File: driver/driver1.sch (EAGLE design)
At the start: 86 parts, among them IC3 74HC14N, IC4 74HC08N, IC5 74HC74N

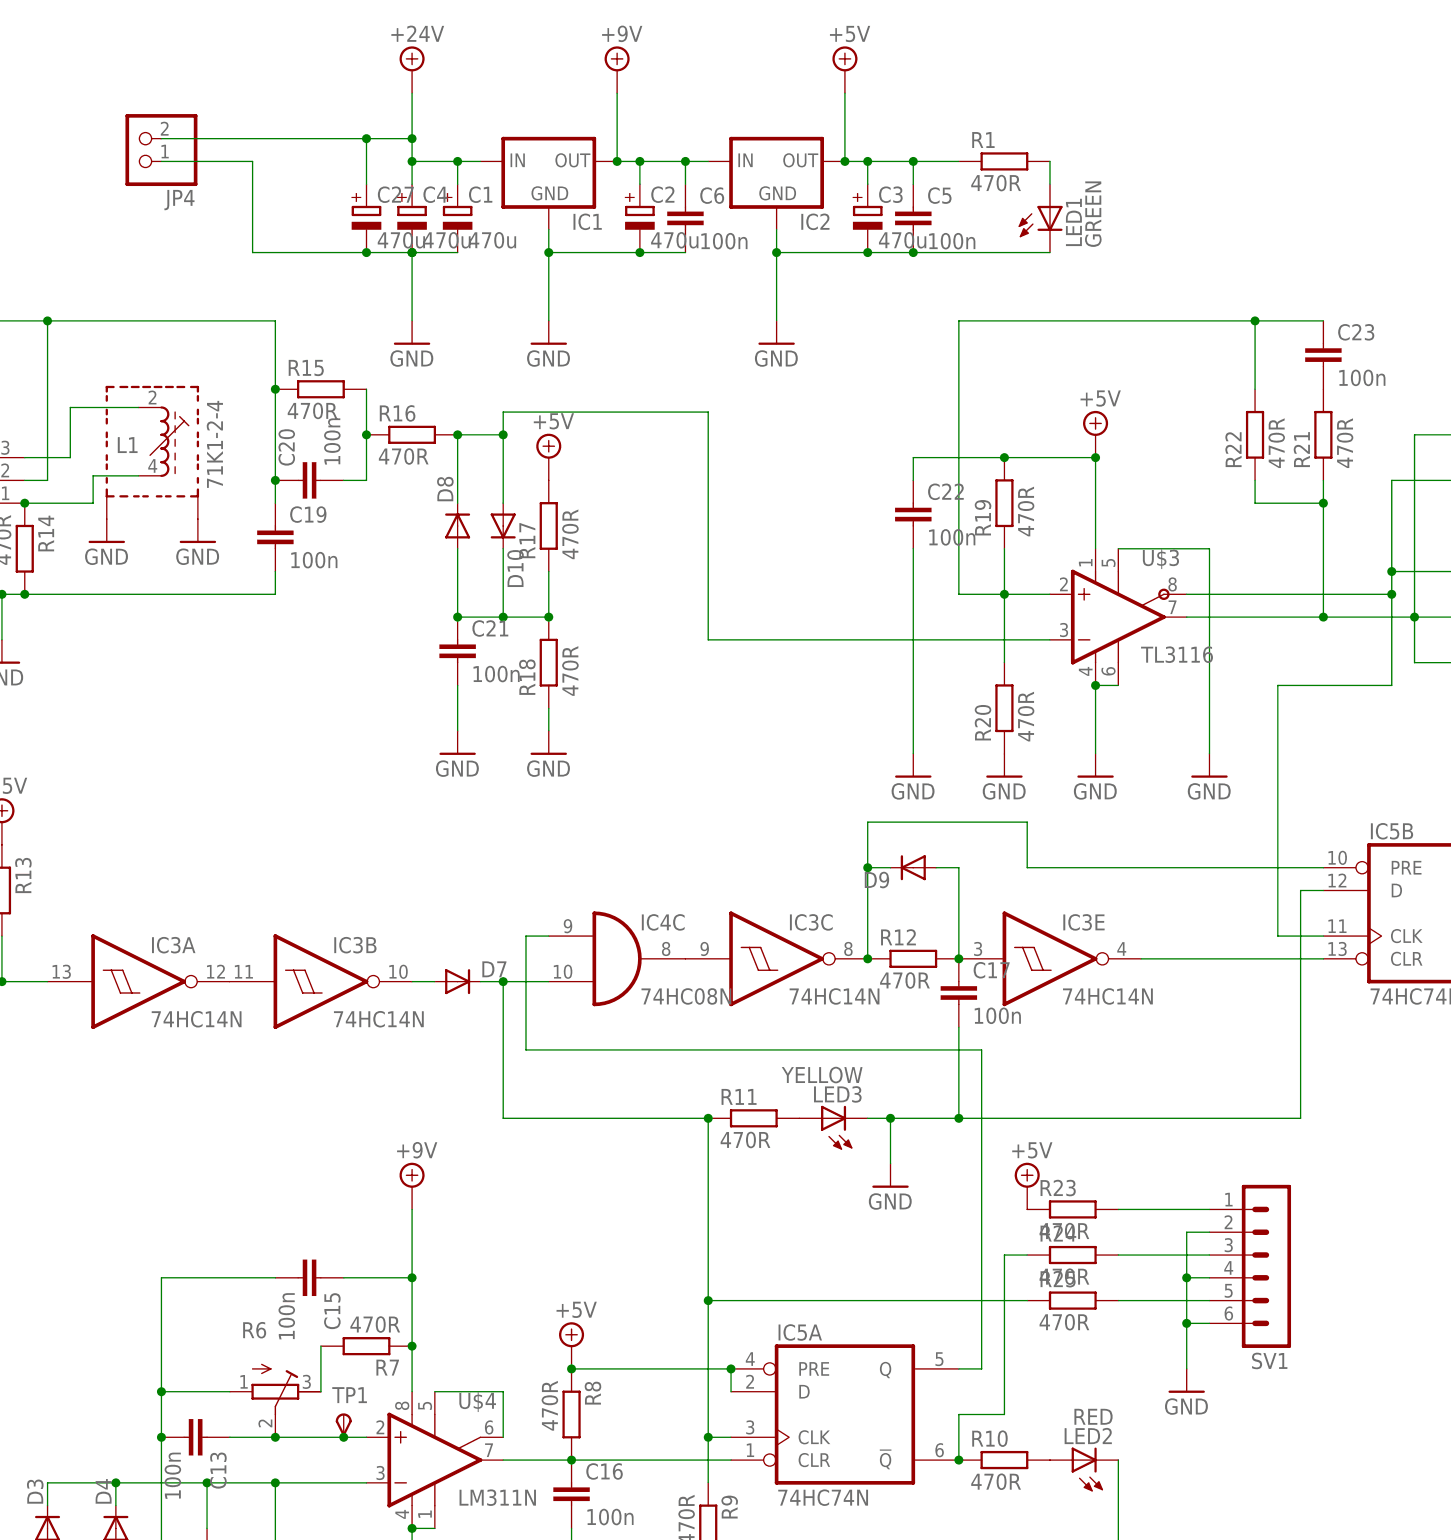
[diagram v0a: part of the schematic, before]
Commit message: improved board layout for use with recom switching 78xx regulators
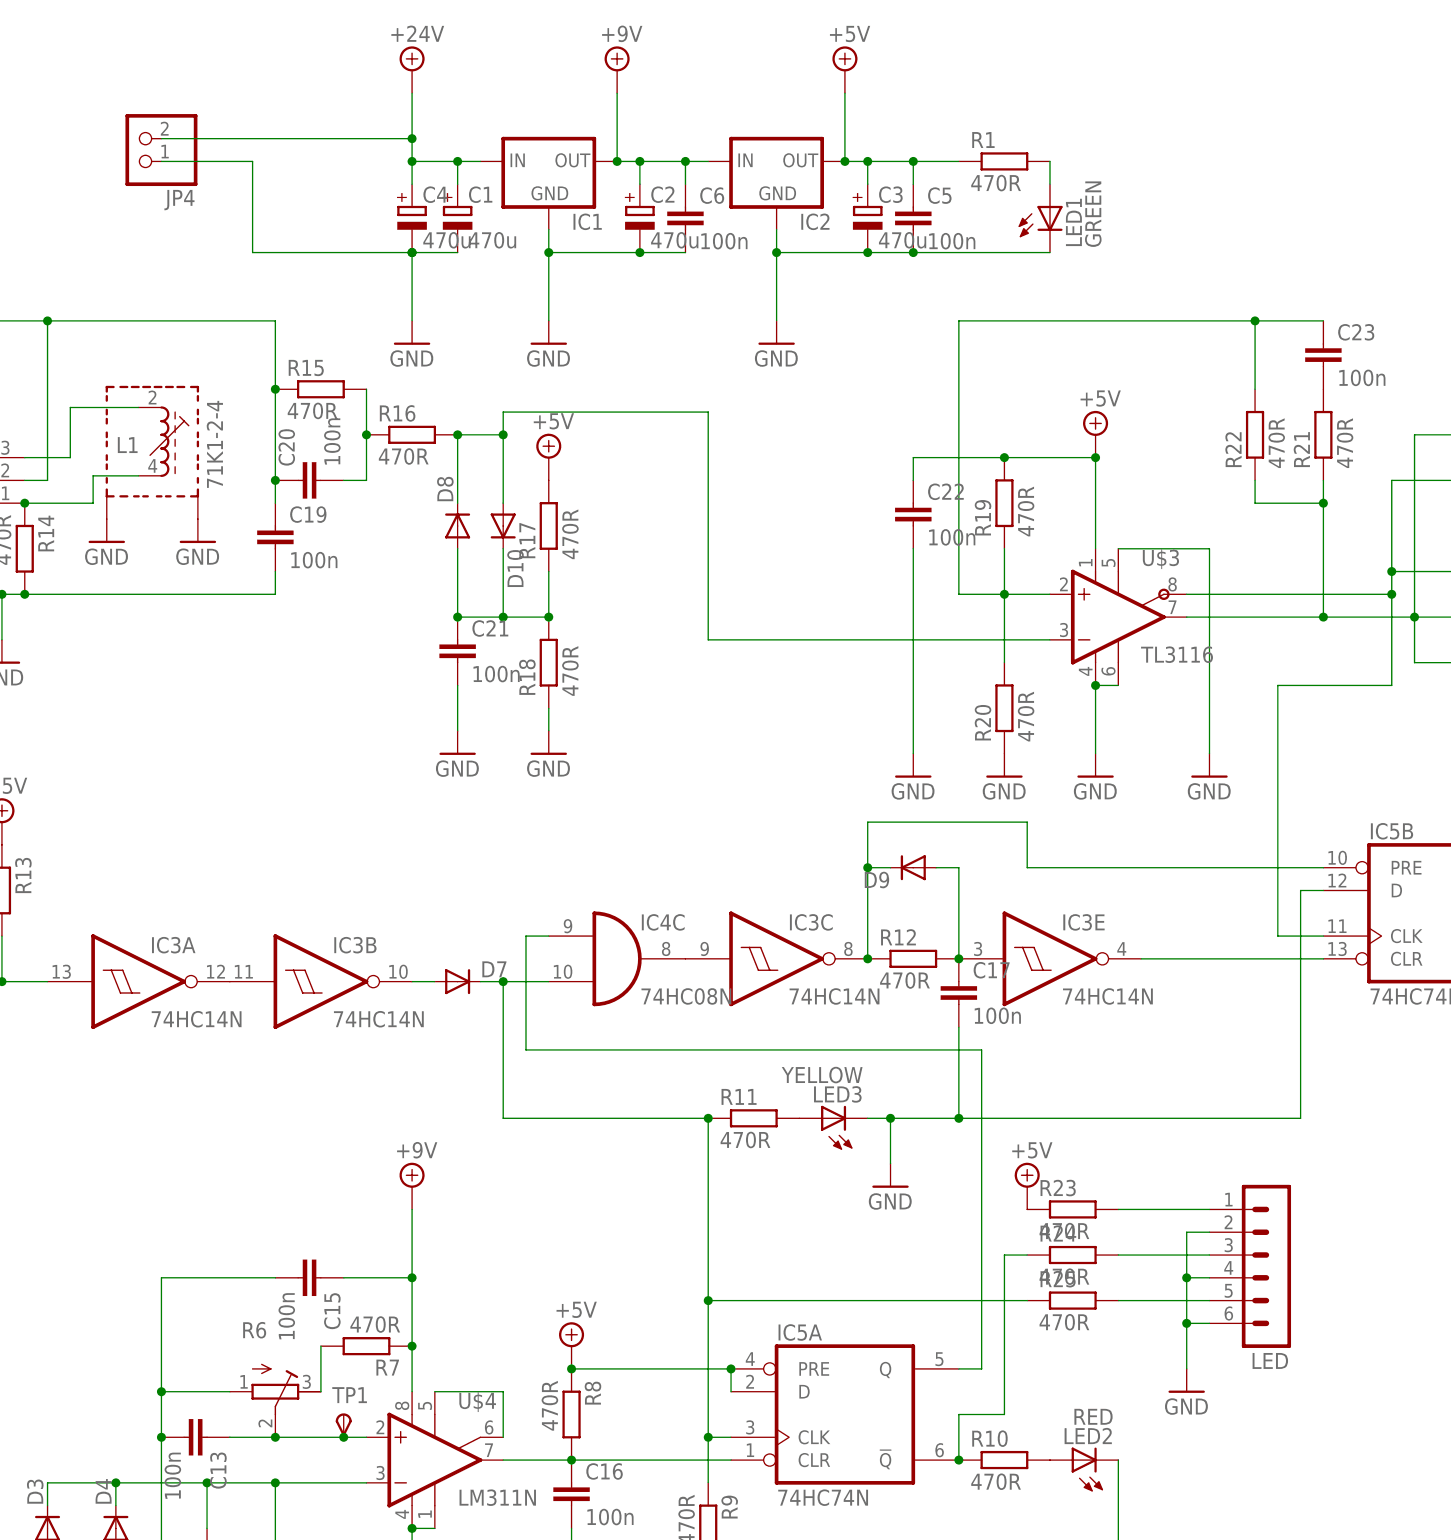
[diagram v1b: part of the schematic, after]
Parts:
- removed C27: 470u, rcl:CPOL-EUE5-8.5
- renumbered SV1 to LED
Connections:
- net +24V: no longer C27.+
- net GND: no longer C27.-
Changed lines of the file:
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@@
 <part name="GND30" library="supply1" deviceset="GND" device=""/>
 <part name="GND31" library="supply1" deviceset="GND" device=""/>
-<part name="SV1" library="con-lstb" deviceset="MA06-1" device=""/>
+<part name="LED" library="con-lstb" deviceset="MA06-1" device=""/>
 <part name="R23" library="rcl" deviceset="R-EU_" device="0207/7" value="470R"/>
 <part name="R24" library="rcl" deviceset="R-EU_" device="0207/7" value="470R"/>
@@
 <part name="GND32" library="supply1" deviceset="GND" device=""/>
 <part name="SUPPLY16" library="supply2" deviceset="+5V" device=""/>
-<part name="C27" library="rcl" deviceset="CPOL-EU" device="E5-8.5" value="470u"/>
 </parts>
 <sheets>
@@
 <instance part="GND30" gate="1" x="-11.176" y="71.882"/>
 <instance part="GND31" gate="1" x="-1.016" y="71.882"/>
-<instance part="SV1" gate="1" x="119.38" y="-10.16" rot="R180"/>
+<instance part="LED" gate="1" x="119.38" y="-10.16" rot="R180"/>
 <instance part="R23" gate="G$1" x="96.52" y="-2.54"/>
 <instance part="R24" gate="G$1" x="96.52" y="-7.62"/>
@@
 <instance part="GND32" gate="1" x="109.22" y="-22.86"/>
 <instance part="SUPPLY16" gate="+5V" x="91.44" y="0"/>
-<instance part="C27" gate="G$1" x="17.78" y="109.22"/>
 </instances>
 <busses>
@@
 <wire x1="-5.08" y1="114.3" x2="5.08" y2="114.3" width="0.1524" layer="91"/>
 <wire x1="5.08" y1="114.3" x2="5.08" y2="104.14" width="0.1524" layer="91"/>
-<wire x1="5.08" y1="104.14" x2="17.78" y2="104.14" width="0.1524" layer="91"/>
+<wire x1="5.08" y1="104.14" x2="22.86" y2="104.14" width="0.1524" layer="91"/>
 <junction x="22.86" y="104.14"/>
-<pinref part="C27" gate="G$1" pin="-"/>
-<wire x1="17.78" y1="104.14" x2="22.86" y2="104.14" width="0.1524" layer="91"/>
-<junction x="17.78" y="104.14"/>
 </segment>
 <segment>
@@
 </segment>
 <segment>
-<pinref part="SV1" gate="1" pin="2"/>
+<pinref part="LED" gate="1" pin="2"/>
 <wire x1="111.76" y1="-5.08" x2="109.22" y2="-5.08" width="0.1524" layer="91"/>
 <pinref part="GND32" gate="1" pin="GND"/>
 <wire x1="109.22" y1="-5.08" x2="109.22" y2="-10.16" width="0.1524" layer="91"/>
-<pinref part="SV1" gate="1" pin="6"/>
+<pinref part="LED" gate="1" pin="6"/>
 <wire x1="109.22" y1="-10.16" x2="109.22" y2="-15.24" width="0.1524" layer="91"/>
 <wire x1="109.22" y1="-15.24" x2="109.22" y2="-20.32" width="0.1524" layer="91"/>
 <wire x1="111.76" y1="-15.24" x2="109.22" y2="-15.24" width="0.1524" layer="91"/>
 <junction x="109.22" y="-15.24"/>
-<pinref part="SV1" gate="1" pin="4"/>
+<pinref part="LED" gate="1" pin="4"/>
 <wire x1="111.76" y1="-10.16" x2="109.22" y2="-10.16" width="0.1524" layer="91"/>
 <junction x="109.22" y="-10.16"/>
@@
 <junction x="27.94" y="114.3"/>
 <pinref part="JP4" gate="G$1" pin="2"/>
-<wire x1="-5.08" y1="116.84" x2="17.78" y2="116.84" width="0.1524" layer="91"/>
+<wire x1="-5.08" y1="116.84" x2="22.86" y2="116.84" width="0.1524" layer="91"/>
 <junction x="22.86" y="116.84"/>
-<pinref part="C27" gate="G$1" pin="+"/>
-<wire x1="17.78" y1="116.84" x2="22.86" y2="116.84" width="0.1524" layer="91"/>
-<wire x1="17.78" y1="116.84" x2="17.78" y2="111.76" width="0.1524" layer="91"/>
-<junction x="17.78" y="116.84"/>
 </segment>
 <segment>
@@
 <net name="N$15" class="0">
 <segment>
-<pinref part="SV1" gate="1" pin="1"/>
+<pinref part="LED" gate="1" pin="1"/>
 <pinref part="R23" gate="G$1" pin="2"/>
 <wire x1="111.76" y1="-2.54" x2="101.6" y2="-2.54" width="0.1524" layer="91"/>
@@
 <net name="N$16" class="0">
 <segment>
-<pinref part="SV1" gate="1" pin="3"/>
+<pinref part="LED" gate="1" pin="3"/>
 <pinref part="R24" gate="G$1" pin="2"/>
 <wire x1="111.76" y1="-7.62" x2="101.6" y2="-7.62" width="0.1524" layer="91"/>
@@
 <net name="N$18" class="0">
 <segment>
-<pinref part="SV1" gate="1" pin="5"/>
+<pinref part="LED" gate="1" pin="5"/>
 <pinref part="R25" gate="G$1" pin="2"/>
 <wire x1="111.76" y1="-12.7" x2="101.6" y2="-12.7" width="0.1524" layer="91"/>

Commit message: guess what.. pcb improvements
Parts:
- R14: device rcl:R-EU_0207/7 -> rcl:R-EU_0309/12
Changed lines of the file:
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@@
 <part name="C18" library="rcl" deviceset="C-EU" device="025-025X050" value="100n"/>
 <part name="GND16" library="supply1" deviceset="GND" device=""/>
-<part name="R14" library="rcl" deviceset="R-EU_" device="0207/7" value="470R"/>
+<part name="R14" library="rcl" deviceset="R-EU_" device="0309/12" value="470R"/>
 <part name="SV2" library="con-lstb" deviceset="MA03-1" device=""/>
 <part name="C19" library="rcl" deviceset="C-EU" device="025-025X050" value="100n"/>

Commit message: added part values
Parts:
- C11, C7: value 100n -> 4.7u
- C12, C16, C23: value 100n -> 1n
- C13, C22, C9: value 100n -> 1u
- C17: value 100n -> 10n
- C19: value 100n -> 150p
- C8: value 100n -> 2.2u
- R12: value 470R -> 10k
- R13, R16, R17, R19, R2, R3, R8, R9: value 470R -> 1k
- R14: value 470R -> 51
- R15, R22: value 470R -> 100k
- R4: value 470R -> 15
- R5: value 470R -> 5.1
- R6: value (none) -> 10k
- R7: value 470R -> 1.8k
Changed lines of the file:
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@@
 <part name="Q3" library="transistor-power" deviceset="PMOSFET_P" device="TO220BV"/>
 <part name="D1" library="diode" deviceset="1N4148" device="DO35-7"/>
-<part name="R2" library="rcl" deviceset="R-EU_" device="0207/7" value="470R"/>
-<part name="C7" library="rcl" deviceset="C-EU" device="025-025X050" value="100n"/>
-<part name="C8" library="rcl" deviceset="C-EU" device="025-025X050" value="100n"/>
-<part name="R4" library="rcl" deviceset="R-EU_" device="0207/7" value="470R"/>
-<part name="C9" library="rcl" deviceset="C-EU" device="025-025X050" value="100n"/>
+<part name="R2" library="rcl" deviceset="R-EU_" device="0207/7" value="1k"/>
+<part name="C7" library="rcl" deviceset="C-EU" device="025-025X050" value="4.7u"/>
+<part name="C8" library="rcl" deviceset="C-EU" device="025-025X050" value="2.2u"/>
+<part name="R4" library="rcl" deviceset="R-EU_" device="0207/7" value="15"/>
+<part name="C9" library="rcl" deviceset="C-EU" device="025-025X050" value="1u"/>
 <part name="C10" library="rcl" deviceset="C-EU" device="025-025X050" value="100n"/>
 <part name="SUPPLY4" library="supply2" deviceset="+24V" device=""/>
@@
 <part name="Q4" library="transistor-power" deviceset="PMOSFET_P" device="TO220BV"/>
 <part name="D2" library="diode" deviceset="1N4148" device="DO35-7"/>
-<part name="R3" library="rcl" deviceset="R-EU_" device="0207/7" value="470R"/>
-<part name="C11" library="rcl" deviceset="C-EU" device="025-025X050" value="100n"/>
+<part name="R3" library="rcl" deviceset="R-EU_" device="0207/7" value="1k"/>
+<part name="C11" library="rcl" deviceset="C-EU" device="025-025X050" value="4.7u"/>
 <part name="C14" library="rcl" deviceset="C-EU" device="025-025X050" value="100n"/>
 <part name="SUPPLY5" library="supply2" deviceset="+24V" device=""/>
@@
 <part name="D5" library="diode" deviceset="DIODE-" device="D-7.5"/>
 <part name="D6" library="diode" deviceset="DIODE-" device="D-7.5"/>
-<part name="C12" library="rcl" deviceset="C-EU" device="025-025X050" value="100n"/>
-<part name="R5" library="rcl" deviceset="R-EU_" device="0309/12" value="470R"/>
+<part name="C12" library="rcl" deviceset="C-EU" device="025-025X050" value="1n"/>
+<part name="R5" library="rcl" deviceset="R-EU_" device="0309/12" value="5.1"/>
 <part name="GND9" library="supply1" deviceset="GND" device=""/>
 <part name="SUPPLY7" library="supply2" deviceset="+9V" device=""/>
-<part name="R6" library="rcl" deviceset="R-TRIMM" device="64W"/>
-<part name="R7" library="rcl" deviceset="R-EU_" device="0207/7" value="470R"/>
-<part name="C13" library="rcl" deviceset="C-EU" device="025-025X050" value="100n"/>
+<part name="R6" library="rcl" deviceset="R-TRIMM" device="64W" value="10k"/>
+<part name="R7" library="rcl" deviceset="R-EU_" device="0207/7" value="1.8k"/>
+<part name="C13" library="rcl" deviceset="C-EU" device="025-025X050" value="1u"/>
 <part name="C15" library="rcl" deviceset="C-EU" device="025-025X050" value="100n"/>
 <part name="GND10" library="supply1" deviceset="GND" device=""/>
-<part name="C16" library="rcl" deviceset="C-EU" device="025-025X050" value="100n"/>
-<part name="R8" library="rcl" deviceset="R-EU_" device="0207/7" value="470R"/>
+<part name="C16" library="rcl" deviceset="C-EU" device="025-025X050" value="1n"/>
+<part name="R8" library="rcl" deviceset="R-EU_" device="0207/7" value="1k"/>
 <part name="SUPPLY8" library="supply2" deviceset="+5V" device=""/>
 <part name="GND11" library="supply1" deviceset="GND" device=""/>
-<part name="R9" library="rcl" deviceset="R-EU_" device="0207/7" value="470R"/>
+<part name="R9" library="rcl" deviceset="R-EU_" device="0207/7" value="1k"/>
 <part name="GND12" library="supply1" deviceset="GND" device=""/>
 <part name="D7" library="diode" deviceset="DIODE-" device="D-7.5"/>
@@
 <part name="GND14" library="supply1" deviceset="GND" device=""/>
 <part name="D9" library="diode" deviceset="DIODE-" device="D-7.5"/>
-<part name="R12" library="rcl" deviceset="R-EU_" device="0207/7" value="470R"/>
-<part name="C17" library="rcl" deviceset="C-EU" device="025-025X050" value="100n"/>
+<part name="R12" library="rcl" deviceset="R-EU_" device="0207/7" value="10k"/>
+<part name="C17" library="rcl" deviceset="C-EU" device="025-025X050" value="10n"/>
 <part name="U$2" library="BillPorter" deviceset="IFD95" device=""/>
 <part name="SUPPLY9" library="supply2" deviceset="+5V" device=""/>
-<part name="R13" library="rcl" deviceset="R-EU_" device="0207/7" value="470R"/>
+<part name="R13" library="rcl" deviceset="R-EU_" device="0207/7" value="1k"/>
 <part name="SUPPLY10" library="supply2" deviceset="+5V" device=""/>
 <part name="GND15" library="supply1" deviceset="GND" device=""/>
 <part name="C18" library="rcl" deviceset="C-EU" device="025-025X050" value="100n"/>
 <part name="GND16" library="supply1" deviceset="GND" device=""/>
-<part name="R14" library="rcl" deviceset="R-EU_" device="0309/12" value="470R"/>
+<part name="R14" library="rcl" deviceset="R-EU_" device="0309/12" value="51"/>
 <part name="SV2" library="con-lstb" deviceset="MA03-1" device=""/>
-<part name="C19" library="rcl" deviceset="C-EU" device="025-025X050" value="100n"/>
-<part name="R15" library="rcl" deviceset="R-EU_" device="0207/7" value="470R"/>
+<part name="C19" library="rcl" deviceset="C-EU" device="025-025X050" value="150p"/>
+<part name="R15" library="rcl" deviceset="R-EU_" device="0207/7" value="100k"/>
 <part name="C20" library="rcl" deviceset="C-EU" device="025-025X050" value="100n"/>
-<part name="R16" library="rcl" deviceset="R-EU_" device="0207/7" value="470R"/>
+<part name="R16" library="rcl" deviceset="R-EU_" device="0207/7" value="1k"/>
 <part name="D8" library="diode" deviceset="DIODE-" device="D-7.5"/>
 <part name="D10" library="diode" deviceset="DIODE-" device="D-7.5"/>
 <part name="C21" library="rcl" deviceset="C-EU" device="025-025X050" value="100n"/>
-<part name="R17" library="rcl" deviceset="R-EU_" device="0207/7" value="470R"/>
+<part name="R17" library="rcl" deviceset="R-EU_" device="0207/7" value="1k"/>
 <part name="SUPPLY11" library="supply2" deviceset="+5V" device=""/>
 <part name="R18" library="rcl" deviceset="R-EU_" device="0207/7" value="470R"/>
@@
 <part name="GND18" library="supply1" deviceset="GND" device=""/>
 <part name="U$3" library="driver" deviceset="TL3116" device=""/>
-<part name="R19" library="rcl" deviceset="R-EU_" device="0207/7" value="470R"/>
+<part name="R19" library="rcl" deviceset="R-EU_" device="0207/7" value="1k"/>
 <part name="R20" library="rcl" deviceset="R-EU_" device="0207/7" value="470R"/>
 <part name="GND19" library="supply1" deviceset="GND" device=""/>
 <part name="GND20" library="supply1" deviceset="GND" device=""/>
 <part name="SUPPLY12" library="supply2" deviceset="+5V" device=""/>
-<part name="C22" library="rcl" deviceset="C-EU" device="025-025X050" value="100n"/>
+<part name="C22" library="rcl" deviceset="C-EU" device="025-025X050" value="1u"/>
 <part name="GND21" library="supply1" deviceset="GND" device=""/>
 <part name="GND22" library="supply1" deviceset="GND" device=""/>
 <part name="R21" library="rcl" deviceset="R-EU_" device="0207/7" value="470R"/>
-<part name="R22" library="rcl" deviceset="R-EU_" device="0207/7" value="470R"/>
-<part name="C23" library="rcl" deviceset="C-EU" device="025-025X050" value="100n"/>
+<part name="R22" library="rcl" deviceset="R-EU_" device="0207/7" value="100k"/>
+<part name="C23" library="rcl" deviceset="C-EU" device="025-025X050" value="1n"/>
 <part name="JP1" library="pinhead" deviceset="PINHD-1X2" device=""/>
 <part name="JP2" library="pinhead" deviceset="PINHD-1X2" device=""/>
